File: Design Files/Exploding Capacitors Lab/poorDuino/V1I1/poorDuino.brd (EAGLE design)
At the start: 68.6 x 53.3 mm, 30 parts, among them IC1 LD117AS33TR, IC2 LD117AS50TR, X1 POWERSUPPLY_DC21MMX, Y2 CSTCE16M0V53-R0 16MHZ

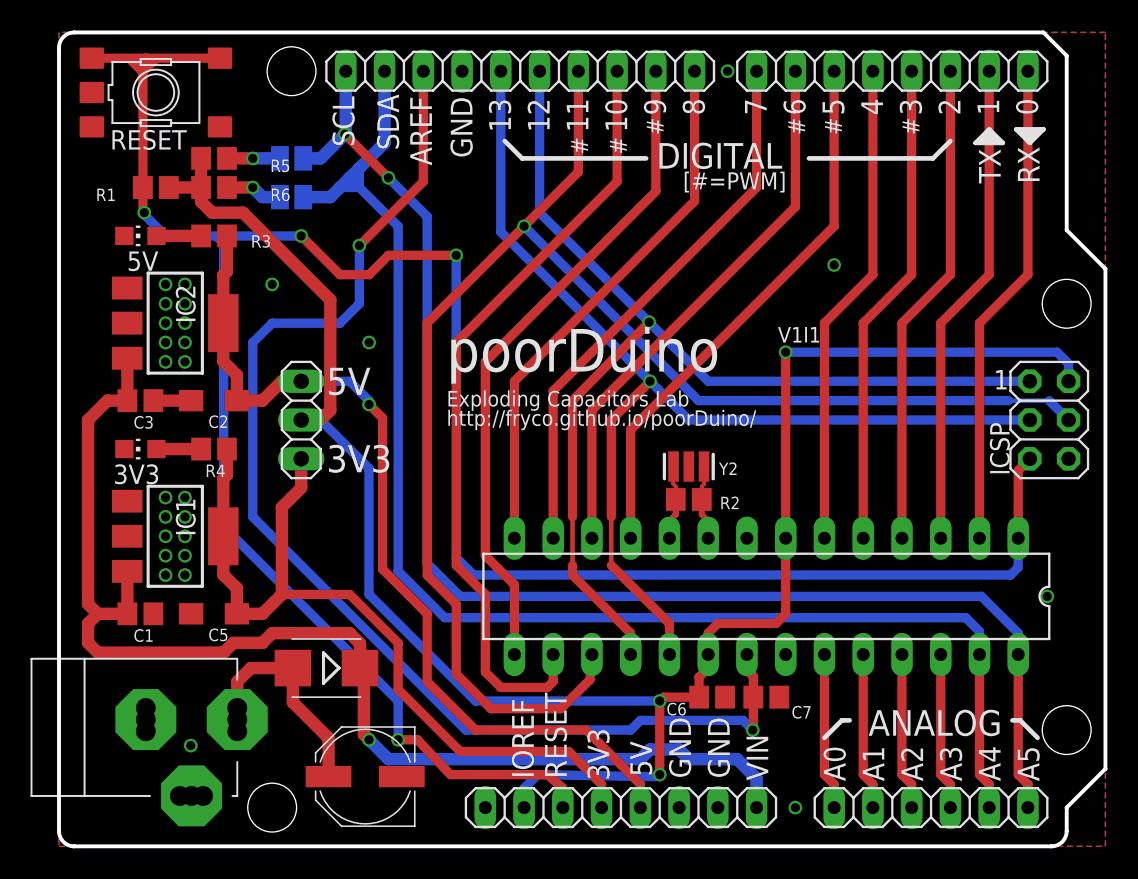
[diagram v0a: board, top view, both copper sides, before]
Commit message: PCB layout improvement
- Better grounding
- Re-alignment of few elements/routes
- Removed useless labels from the bottom of the board
- RCL labels alignment
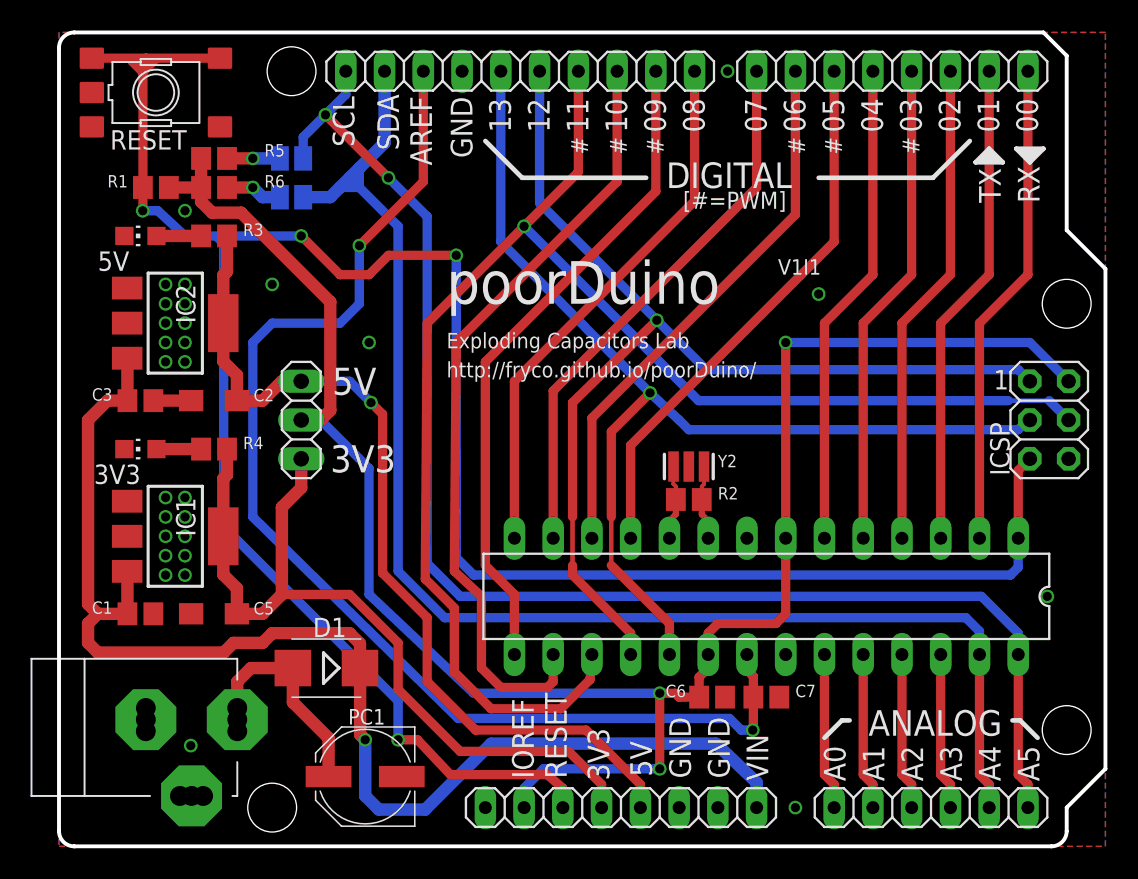
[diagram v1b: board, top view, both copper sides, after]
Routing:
- net VCC: track 80.1 -> 85.6 mm
- net AD5/SCL: track 90.2 -> 91.4 mm
- net AREF: track 80.7 -> 80.1 mm
- net GND: vias 27 -> 28
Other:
- board text added: "00"
- board text added: "01"
- board text added: "02"
- board text added: "03"
- board text added: "04"
- board text added: "05"
- board text added: "06"
- board text added: "07"
- board text added: "08"
- board text added: "09"
- board text removed: "0"
- board text removed: "2"
- board text removed: "3"
- board text removed: "4"
- board text removed: "5"
- board text removed: "6"
- board text removed: "7"
- board text removed: "8"
- board text removed: "9"
- board text removed: "ATMEGA328"
- board text removed: "ITALY"
- board text removed: "MADE IN"
- board text removed: "designed by"
- board text removed: "tinker it"
